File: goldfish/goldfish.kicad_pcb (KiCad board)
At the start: 4 copper layers, 21.3 x 33.9 mm, 25 parts, among them J3 01x12, J4 01x12, J5 01x05, U1 ATmega32U4, X1 16MHz

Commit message: Silk Screen layers cleaned up and labels added.
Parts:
- USB1: value CLEAN-TYPE-C-31-M-12 -> TYPE-C-31-M-12
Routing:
- net VCC: track 19.5 -> 23.7 mm, vias 6 -> 8
- net VBUS: track 30.5 -> 33.6 mm, vias 2 -> 4
- net /PB2: track 20.5 -> 22.3 mm
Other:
- board text added: "+"
- board text added: "Goldfish-clone-JLCPCB Jeremy J Starcher Designed or JLC PCB assembly REV A"
- board text added: "REV A Goldfish-clone-JLCPCB"

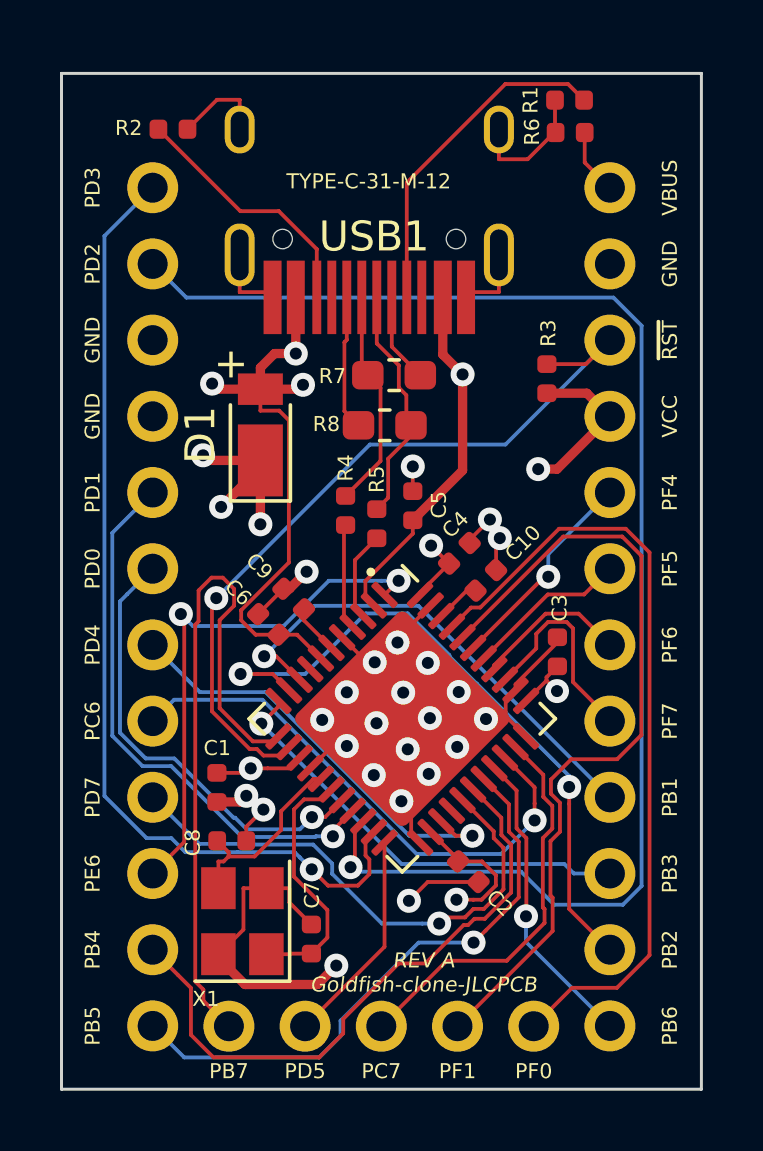
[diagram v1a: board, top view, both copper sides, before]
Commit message: Added header pins to 3d model
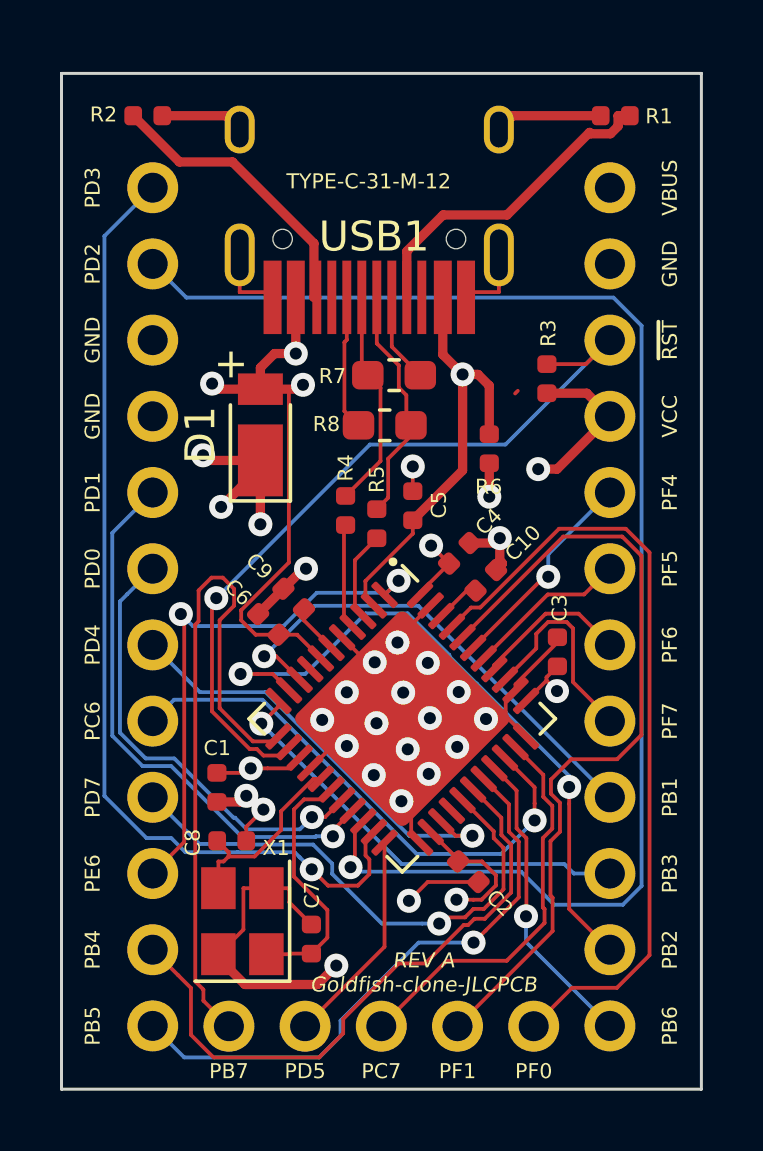
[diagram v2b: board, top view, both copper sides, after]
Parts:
- moved R6 10.9 mm to (33.6, 36.0), turned to 90 degrees
- moved R1 1.61 mm to (37.8, 24.9)
- moved R2 0.95 mm to (22.2, 24.9)
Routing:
- net Net-(R2-Pad2): track 8.54 -> 9.68 mm
- net GND: track 52.7 -> 53.3 mm
- net VBUS: track 33.6 -> 34.3 mm

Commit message: Cleanup after submitting rev-a
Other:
- board text added: "GOLDFISH - JLCPCB This Goldfish clone was designed for the JLCPCB SMD assembly process."
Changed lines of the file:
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@@
   (general
     (thickness 1.6)
-    (drawings 8)
+    (drawings 9)
     (tracks 483)
     (zones 0)
@@
   )
   (page A4)
+  (title_block
+    (title "GoldFish - JLCPCB")
+    (date 2020-11-30)
+    (rev A)
+    (company "Jeremy J Starcher")
+    (comment 1 "Layout designed for JLCPCB assembly process.")
+  )
   (layers
     (0 F.Cu signal)
@@
     )
   )
+  (gr_text "GOLDFISH - JLCPCB\n\nThis Goldfish clone was designed for the JLCPCB SMD assembly process.\n" (at 74.1 25.2) (layer F.Fab)
+    (effects (font (size 1 1) (thickness 0.15)))
+  )
   (gr_text "REV A\nGoldfish-clone-JLCPCB" (at 31.41 53.46) (layer F.SilkS)

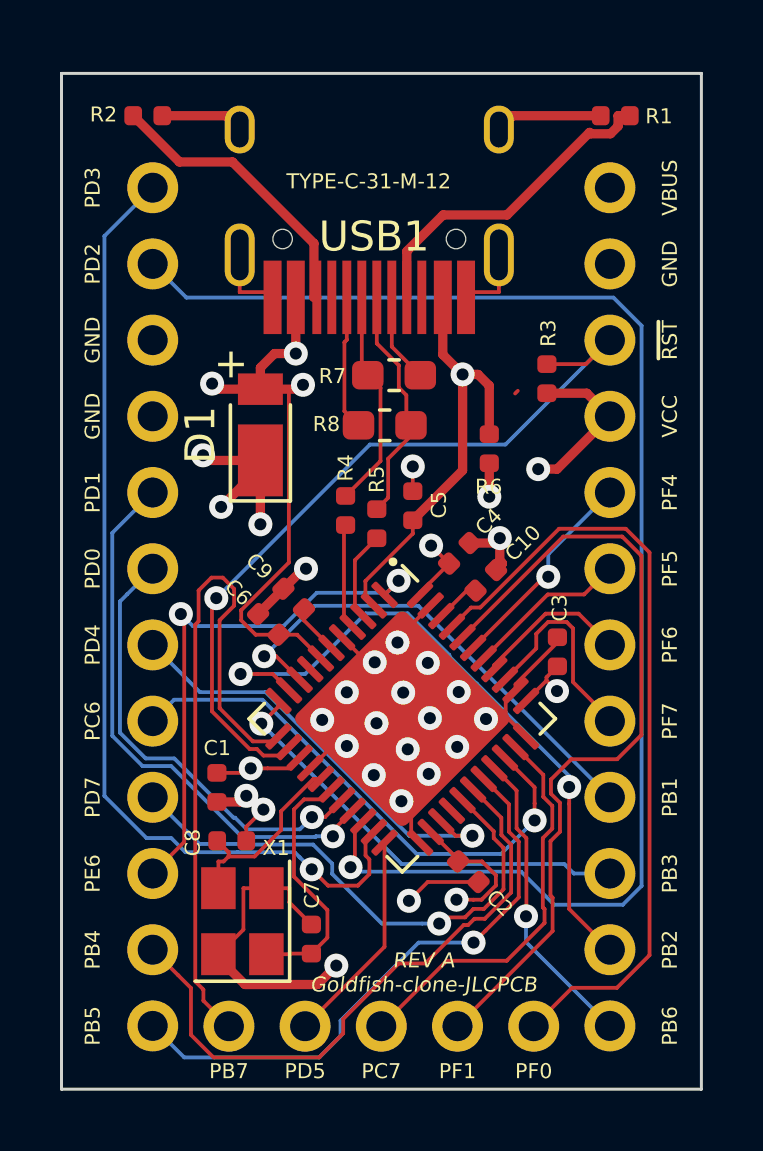
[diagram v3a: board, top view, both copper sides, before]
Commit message: Added the option for a USB-micro breakboard board on the USB as well.
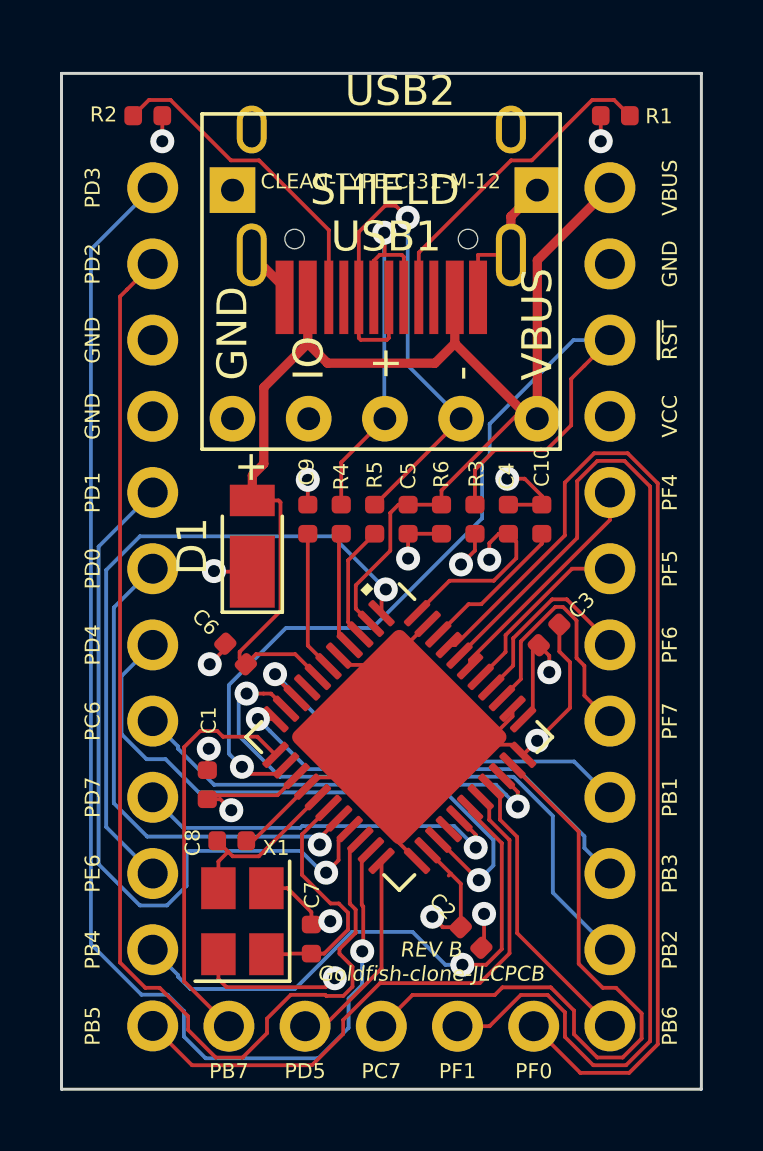
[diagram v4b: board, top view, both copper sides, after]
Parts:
- removed R7, R8: 0R, Resistor_SMD:R_0603_1608Metric_Pad1.05x0.95mm_HandSolder
- added USB2: PIN-USB, pin-usb:pin-usb, F.Cu at (35.2, 35.0)
- USB1: value TYPE-C-31-M-12 -> CLEAN-TYPE-C-31-M-12
- moved R3 5.26 mm to (33.1, 38.4)
- moved D1 3.72 mm to (25.7, 39.2)
- moved R6 2.84 mm to (32.0, 38.4)
- moved C10 2.76 mm to (35.4, 38.4), turned to 90 degrees
- moved C9 2.70 mm to (27.6, 38.4), turned to 90 degrees
- moved C2 2.19 mm to (33.0, 52.3)
- moved C4 1.99 mm to (34.2, 38.4), turned to 90 degrees
- moved C6 1.47 mm to (25.1, 42.8)
- moved C3 0.63 mm to (35.6, 42.2), turned to 45 degrees
- moved U1 0.62 mm to (30.6, 45.6)
- moved C5 0.48 mm to (30.9, 38.4), turned to 270 degrees
- moved USB1 0.40 mm to (30.0, 22.8)
- moved C1 0.33 mm to (24.2, 47.2), turned to 90 degrees
- moved R4 0.32 mm to (28.7, 38.4)
- moved R5 0.17 mm to (29.8, 38.4)
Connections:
- USB1 pad 5: Net-(R7-Pad2) -> /D+
- USB1 pad 8: Net-(R8-Pad2) -> /D-
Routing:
- net VBUS: track 34.3 -> 47.3 mm, vias 4 -> 0
- net /D-: track 7.53 -> 19.6 mm, vias 0 -> 1
- net /PD3: track 32.7 -> 43.4 mm
- net /PF1: track 27.0 -> 37.6 mm
- net /PB7: track 23.2 -> 13.5 mm
- net /PC7: track 13.4 -> 22.1 mm
- net /PF0: track 26.5 -> 34.9 mm
- net /PD2: track 48.0 -> 39.9 mm, vias 1 -> 0
- net /D+: track 7.36 -> 14.1 mm, vias 0 -> 1
- net /PD1: track 18.6 -> 24.8 mm
- net /PD4: track 14.5 -> 20.7 mm
- net /RESET: track 26.2 -> 32.1 mm
- net /PD7: track 17.6 -> 12.7 mm
- net Net-(R8-Pad2): track 4.49 -> 0.00 mm
- net /PE6: track 17.8 -> 22.1 mm, vias 2 -> 1
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- removed copper zone on In1.Cu, net VBUS
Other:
- board text added: "REV B Goldfish-clone-JLCPCB"
- board text added: "https://github.com/ JeremyJStarcher/ Goldfish-clone-JLCPCB Designed for JLC PCB assembly REV B"
- board text removed: "+"
- board text removed: "Goldfish-clone-JLCPCB Jeremy J Starcher Designed or JLC PCB assembly REV A"
- board text removed: "REV A Goldfish-clone-JLCPCB"
